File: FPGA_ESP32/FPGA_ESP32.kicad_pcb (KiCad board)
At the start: 2 copper layers, 24.8 x 24.8 mm, 56 parts, among them J1 Conn_01x14_Female, J3 Conn_01x14_Female, J4 Conn_01x14_Female, J5 Conn_01x14_Female, U1 LFE5UM-25F-7MG285C, U10 GD25Q16CEIGR, U2 ESP32-PICO-D4, U3 TLV71211_SOT23-5, U4 W956D6KBKX, U5 TW9900, U6 W956D6KBKX, U7 RFX2411, U8 SPX3819M5-L-1-8, U9 SPX3819M5-L-2-5, Y1 Crystal_GND23

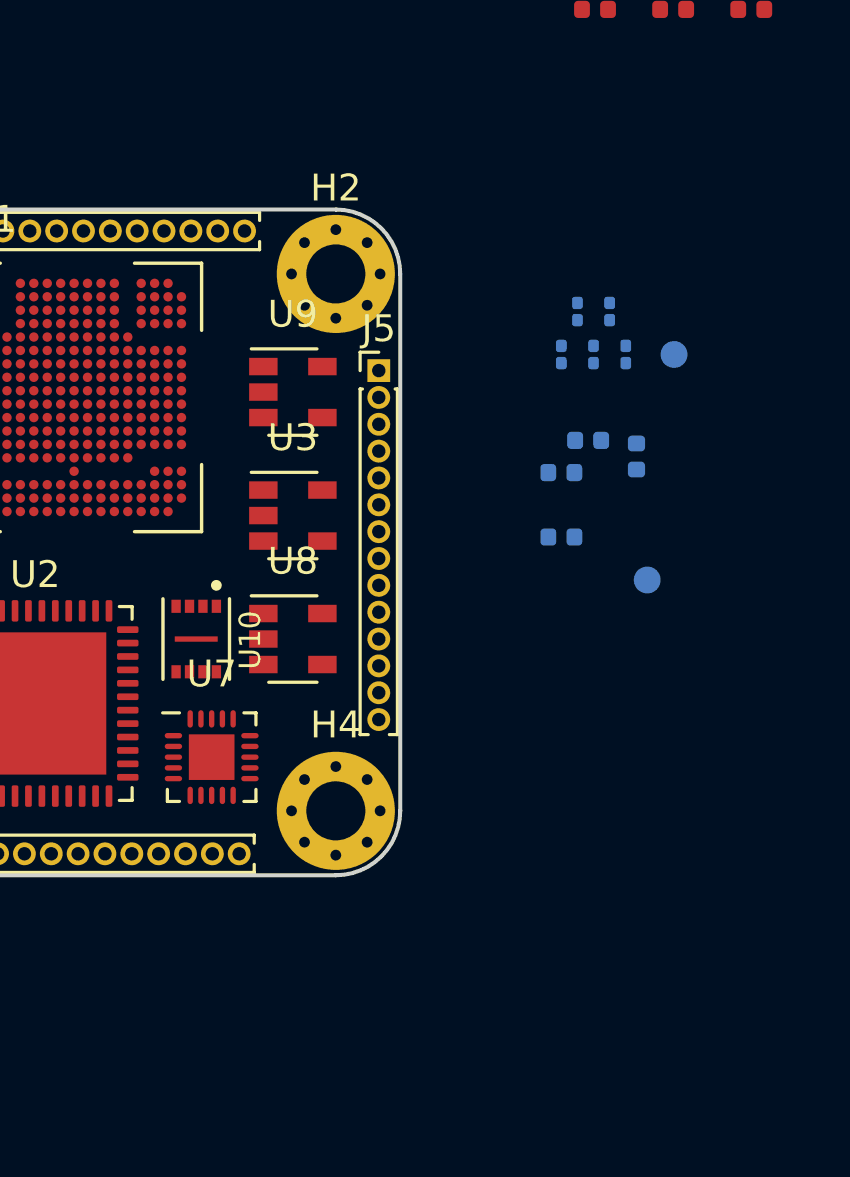
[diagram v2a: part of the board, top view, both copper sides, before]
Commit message: FPGA_ESP32 : power done, antenna matching done, todo crystal and capacitor purge
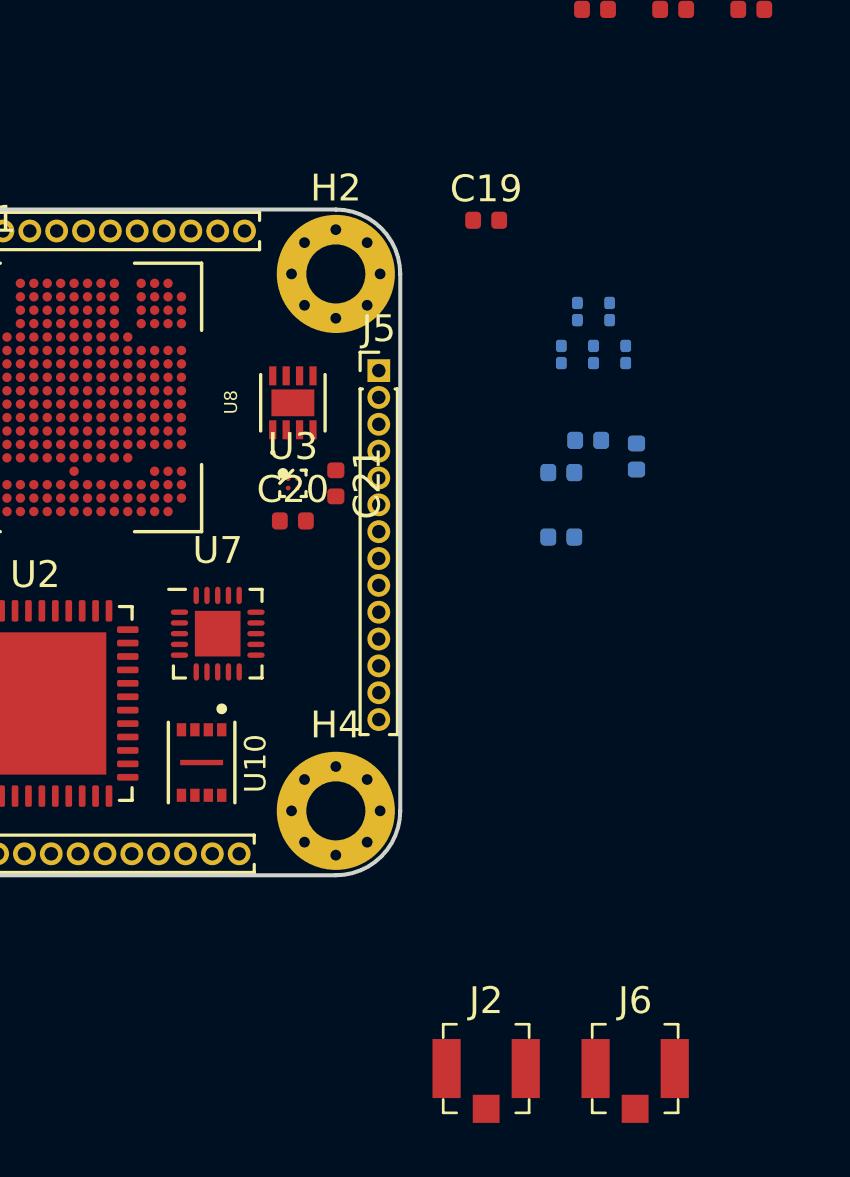
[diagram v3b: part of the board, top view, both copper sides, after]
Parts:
- removed ANT1, ANT2: Antenna, TestPoint:TestPoint_Pad_D1.0mm
- removed U9: SPX3819M5-L-2-5, Package_TO_SOT_SMD:SOT-23-5
- added C19: 1uF, Capacitor_SMD:C_0402_1005Metric, F.Cu at (75.6, 18.0)
- added C20: 1uF, Capacitor_SMD:C_0402_1005Metric, F.Cu at (68.4, 29.2)
- added C21: 1uF, Capacitor_SMD:C_0402_1005Metric, F.Cu at (70.0, 27.8)
- added J2: U_FL-R-SMT_10_, digikey-footprints:Coax_Conn_U.FL, F.Cu at (75.6, 49.6)
- added J6: U_FL-R-SMT_10_, digikey-footprints:Coax_Conn_U.FL, F.Cu at (81.2, 49.6)
- C12: value C -> 3.9pF
- C13: value C -> 2.4pF
- L2: value L -> 2.7N
- U3: value TLV71211_SOT23-5 -> LP5910; footprint Package_TO_SOT_SMD:SOT-23-5 -> footprints:BGA-4_2x2_0.74x0.74mm
- U8: value SPX3819M5-L-1-8 -> ADP222ACPZ-1825-R7; footprint Package_TO_SOT_SMD:SOT-23-5 -> footprints:SON50P200X200X60-9N
- moved U8 8.80 mm to (68.4, 24.8), turned to 90 degrees
- moved U7 4.61 mm to (65.6, 33.4)
- moved U10 4.60 mm to (65.0, 38.2)
- moved U3 1.20 mm to (68.4, 27.8)
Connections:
- U8 pad 1: Net-(U8-Pad1) -> VIO
- U8 pad 2: Net-(U8-Pad2) -> VIO
- U8 pad 3: Net-(U8-Pad3) -> GND
- U8 pad 4: Net-(U8-Pad4) -> +2V5
- U8 pad 5: Net-(U8-Pad5) -> +2V5

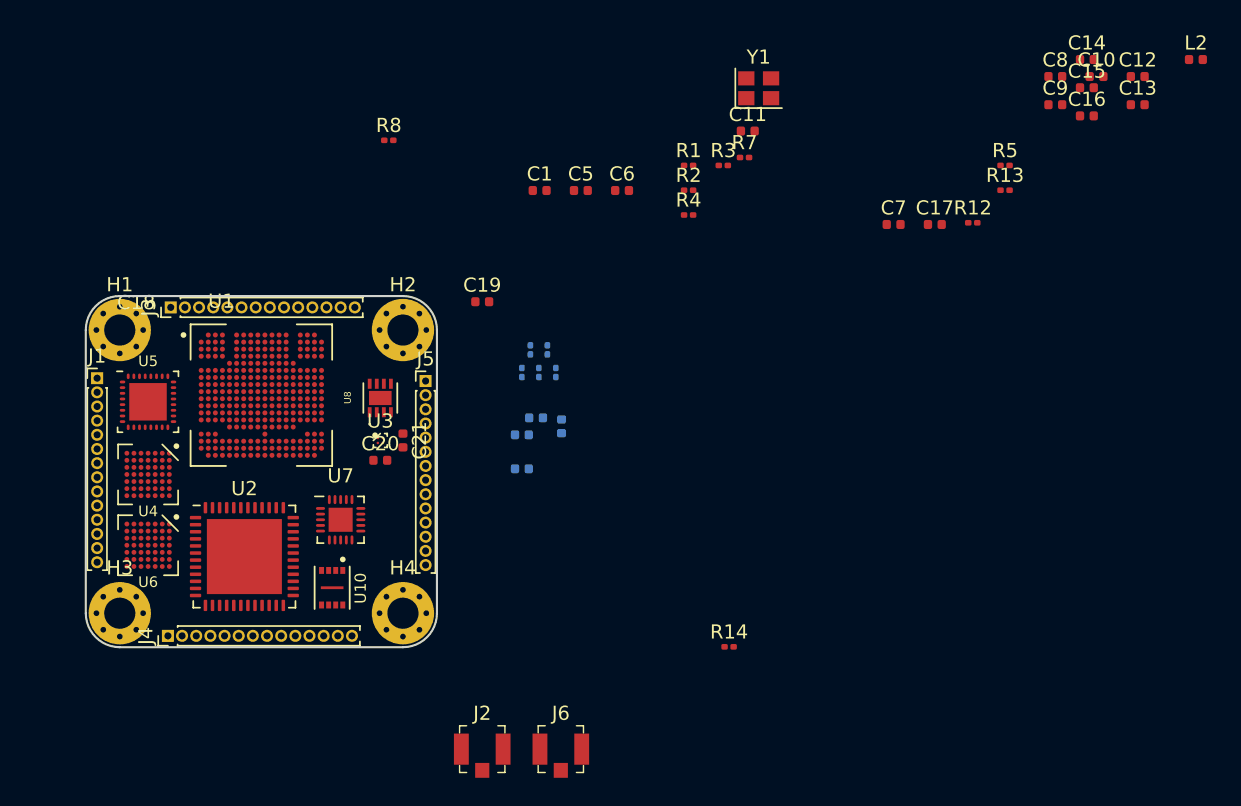
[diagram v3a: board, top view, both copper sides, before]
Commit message: FPGA_ESP32 : esp32/rf pa+lna+switch routing progress
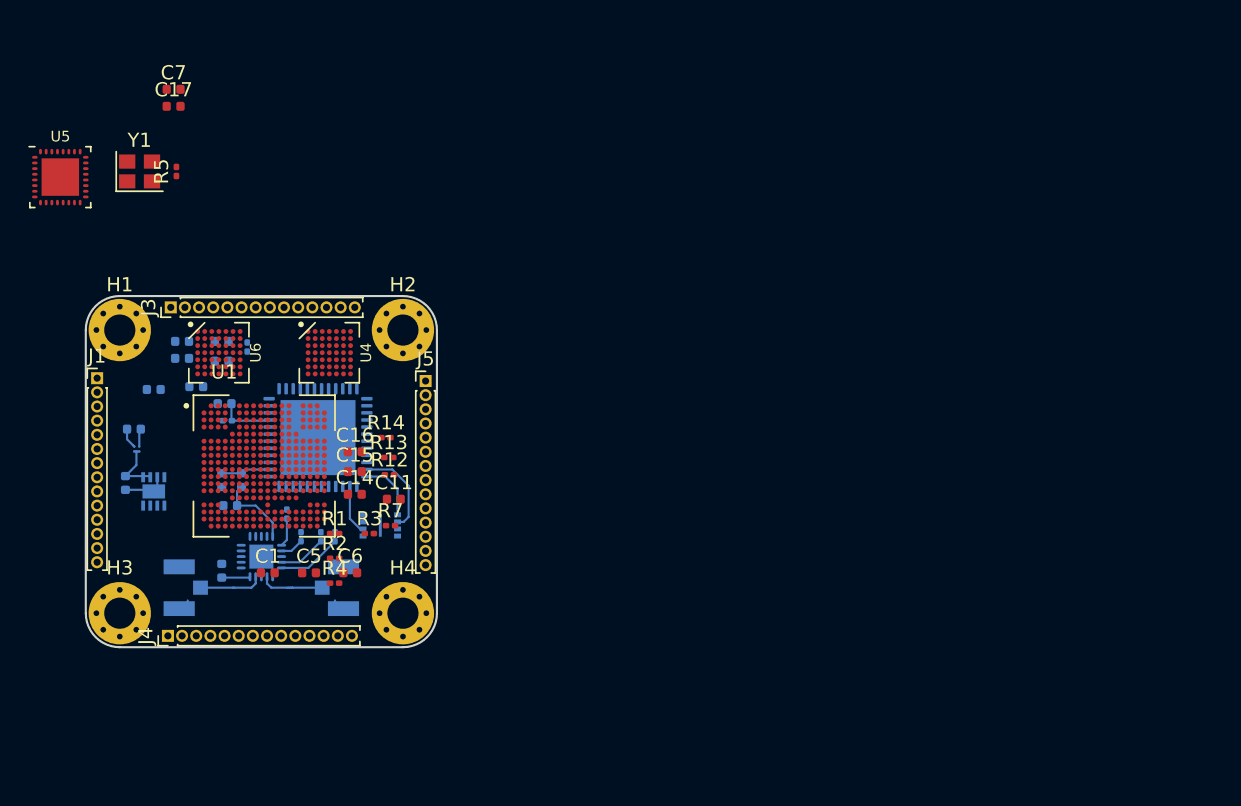
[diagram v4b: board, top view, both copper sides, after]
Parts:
- removed C20: 1uF, Capacitor_SMD:C_0402_1005Metric
- C10, C12, C13, C18, C19, C21, C8, C9, J2, J6, L2, R8, U10, U2, U7, U8: moved to B.Cu
- U3: value LP5910 -> LP5910-1.1BYKAT; moved to B.Cu
- moved L2 74.9 mm to (57.2, 30.6), turned to 270 degrees
- moved C13 70.1 mm to (57.8, 32.4), turned to 180 degrees
- moved C12 69.4 mm to (58.6, 30.6), turned to 270 degrees
- moved C10 64.6 mm to (57.2, 20.8)
- moved C9 63.9 mm to (55.4, 24.0), turned to 180 degrees
- moved C8 62.2 mm to (57.2, 22.2)
- moved C14 60.1 mm to (66.6, 31.6)
- moved R5 58.5 mm to (54.0, 8.80), turned to 90 degrees
- moved C15 58.4 mm to (66.6, 30.0)
- moved C16 56.9 mm to (66.6, 28.6)
- moved C17 54.4 mm to (53.8, 4.20)
- moved C7 51.7 mm to (53.8, 3.00)
- moved R13 47.4 mm to (69.0, 29.0)
- moved R12 44.9 mm to (69.0, 30.2)
- moved Y1 44.1 mm to (51.4, 8.80)
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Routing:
- net /SPI_CLK: track 0.00 -> 6.55 mm
- net GND: track 0.00 -> 5.75 mm
- net /WIFI, BT, RT/TXRX: track 0.00 -> 5.43 mm
- net Net-(J6-Pad2): track 0.00 -> 4.80 mm
- net Net-(J2-Pad2): track 0.00 -> 4.60 mm
- net Net-(R16-Pad1): track 0.00 -> 4.55 mm
- net /SPI_MOSI: track 0.00 -> 4.36 mm
- net VIO: track 0.00 -> 4.19 mm
- net EN: track 0.00 -> 3.87 mm
- net /SPI_MISO: track 0.00 -> 3.50 mm
- net Net-(C12-Pad1): track 0.00 -> 3.46 mm
- net Net-(R17-Pad1): track 0.00 -> 3.39 mm
- net Net-(R19-Pad1): track 0.00 -> 2.04 mm
- net Net-(L1-Pad2): track 0.00 -> 2.02 mm
- net Net-(R18-Pad1): track 0.00 -> 1.66 mm
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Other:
- copper layers 2 -> 4
- net class Default: clearance 0.08 -> 0.06; trace_width 0.15 -> 0.12
- rule trace_clearance: 0.08 -> 0.06
- rule trace_min: 0.15 -> 0.12
